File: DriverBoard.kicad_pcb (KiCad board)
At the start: 2 copper layers, 80 x 60 mm, 105 parts, among them J1 Conn_02x07_Odd_Even, J2 Conn_02x07_Odd_Even, Q1 HYG025N06LS1C2, Q2 HYG025N06LS1C2, Q3 HYG025N06LS1C2, Q4 HYG025N06LS1C2, Q5 HYG025N06LS1C2, Q6 HYG025N06LS1C2, U2 SCT2420, U3 SCT2610

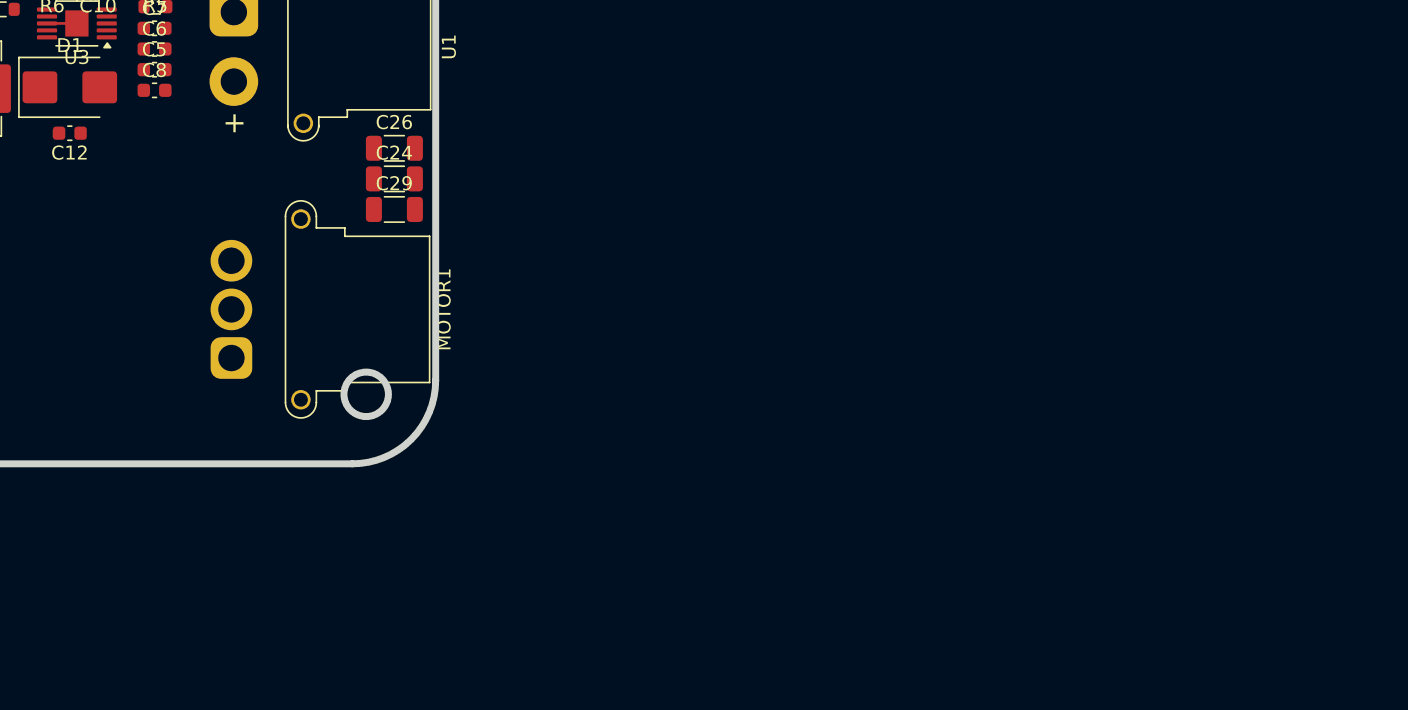
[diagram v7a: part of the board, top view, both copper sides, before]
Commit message: 原理图增加motor2部分
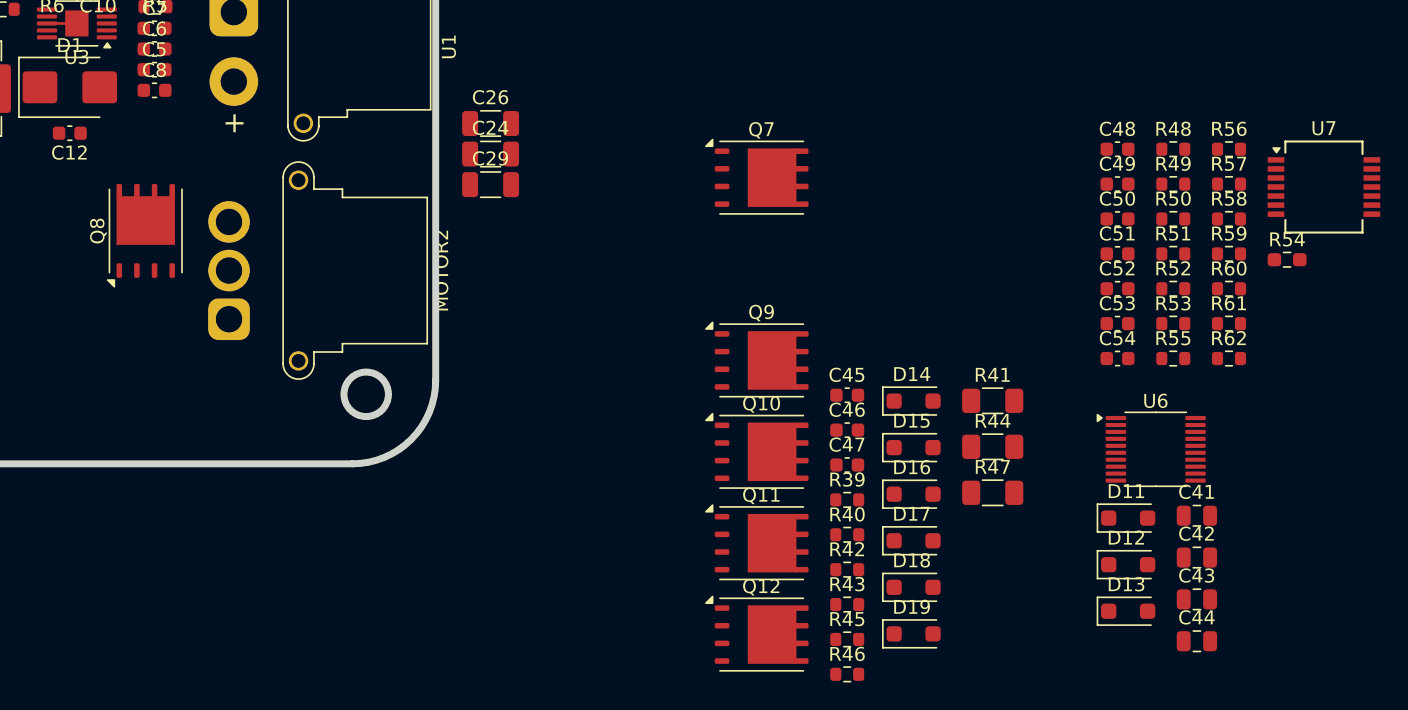
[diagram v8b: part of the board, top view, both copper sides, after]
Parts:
- removed the MOTOR1 at (182.3, 98.6)
- added C41: 0.47uF, Capacitor_SMD:C_0805_2012Metric, F.Cu at (251.7, 109.9)
- added C42: 0.47uF, Capacitor_SMD:C_0805_2012Metric, F.Cu at (251.7, 112.9)
- added C43: 0.47uF, Capacitor_SMD:C_0805_2012Metric, F.Cu at (251.7, 116.0)
- added C44: 0.47uF, Capacitor_SMD:C_0805_2012Metric, F.Cu at (251.7, 119.0)
- added C45: 0.1uF/100V, Capacitor_SMD:C_0603_1608Metric, F.Cu at (226.6, 101.3)
- added C46: 0.1uF/100V, Capacitor_SMD:C_0603_1608Metric, F.Cu at (226.6, 103.8)
- added C47: 0.1uF/100V, Capacitor_SMD:C_0603_1608Metric, F.Cu at (226.6, 106.3)
- added C48: NC, Capacitor_SMD:C_0603_1608Metric, F.Cu at (246.0, 83.6)
- added C49: 1nF, Capacitor_SMD:C_0603_1608Metric, F.Cu at (246.0, 86.1)
- added C50: NC, Capacitor_SMD:C_0603_1608Metric, F.Cu at (246.0, 88.6)
- added C51: NC, Capacitor_SMD:C_0603_1608Metric, F.Cu at (246.0, 91.1)
- added C52: NC, Capacitor_SMD:C_0603_1608Metric, F.Cu at (246.0, 93.6)
- added C53: NC, Capacitor_SMD:C_0603_1608Metric, F.Cu at (246.0, 96.1)
- added C54: NC, Capacitor_SMD:C_0603_1608Metric, F.Cu at (246.0, 98.6)
- added D11: SODF107-SH, Diode_SMD:D_SOD-123F, F.Cu at (246.8, 110.1)
- added D12: SODF107-SH, Diode_SMD:D_SOD-123F, F.Cu at (246.8, 113.5)
- added D13: SODF107-SH, Diode_SMD:D_SOD-123F, F.Cu at (246.8, 116.8)
- added D14: SODF107-SH, Diode_SMD:D_SOD-123F, F.Cu at (231.4, 101.7)
- added D15: SODF107-SH, Diode_SMD:D_SOD-123F, F.Cu at (231.4, 105.0)
- added D16: SODF107-SH, Diode_SMD:D_SOD-123F, F.Cu at (231.4, 108.4)
- added D17: SODF107-SH, Diode_SMD:D_SOD-123F, F.Cu at (231.4, 111.7)
- added D18: SODF107-SH, Diode_SMD:D_SOD-123F, F.Cu at (231.4, 115.1)
- added D19: SODF107-SH, Diode_SMD:D_SOD-123F, F.Cu at (231.4, 118.4)
- added MOTOR2: Conn_01x03, footprints:MR30PW-FB_1x03_P3.50mm_Horizontal, F.Cu at (182.1, 95.8)
- added Q10: HYG025N06LS1C2, footprints:HYG025N06LS1C2-PDFN-8-1EP_6x5mm_P1.27mm_EP3x3mm, F.Cu at (220.4, 105.3)
- added Q11: HYG025N06LS1C2, footprints:HYG025N06LS1C2-PDFN-8-1EP_6x5mm_P1.27mm_EP3x3mm, F.Cu at (220.4, 111.9)
- added Q12: HYG025N06LS1C2, footprints:HYG025N06LS1C2-PDFN-8-1EP_6x5mm_P1.27mm_EP3x3mm, F.Cu at (220.4, 118.5)
- added Q7: HYG025N06LS1C2, footprints:HYG025N06LS1C2-PDFN-8-1EP_6x5mm_P1.27mm_EP3x3mm, F.Cu at (220.4, 85.6)
- added Q8: HYG025N06LS1C2, footprints:HYG025N06LS1C2-PDFN-8-1EP_6x5mm_P1.27mm_EP3x3mm, F.Cu at (176.1, 89.4)
- added Q9: HYG025N06LS1C2, footprints:HYG025N06LS1C2-PDFN-8-1EP_6x5mm_P1.27mm_EP3x3mm, F.Cu at (220.4, 98.8)
- added R39: 100R, Resistor_SMD:R_0603_1608Metric, F.Cu at (226.6, 108.8)
- added R40: 100R, Resistor_SMD:R_0603_1608Metric, F.Cu at (226.6, 111.3)
- added R41: 5mR, Resistor_SMD:R_1206_3216Metric_Pad1.30x1.75mm_HandSolder, F.Cu at (237.0, 101.7)
- added R42: 100R, Resistor_SMD:R_0603_1608Metric, F.Cu at (226.6, 113.8)
- added R43: 100R, Resistor_SMD:R_0603_1608Metric, F.Cu at (226.6, 116.3)
- added R44: 5mR, Resistor_SMD:R_1206_3216Metric_Pad1.30x1.75mm_HandSolder, F.Cu at (237.0, 105.0)
- added R45: 100R, Resistor_SMD:R_0603_1608Metric, F.Cu at (226.6, 118.8)
- added R46: 100R, Resistor_SMD:R_0603_1608Metric, F.Cu at (226.6, 121.3)
- added R47: 5mR, Resistor_SMD:R_1206_3216Metric_Pad1.30x1.75mm_HandSolder, F.Cu at (237.0, 108.3)
- added R48: 4.7K, Resistor_SMD:R_0603_1608Metric, F.Cu at (250.0, 83.6)
- added R49: 4.7K, Resistor_SMD:R_0603_1608Metric, F.Cu at (250.0, 86.1)
- added R50: 6.8K, Resistor_SMD:R_0603_1608Metric, F.Cu at (250.0, 88.6)
- added R51: 1K(1%), Resistor_SMD:R_0603_1608Metric, F.Cu at (250.0, 91.1)
- added R52: 4.7K(1%), Resistor_SMD:R_0603_1608Metric, F.Cu at (250.0, 93.6)
- added R53: 0R, Resistor_SMD:R_0603_1608Metric, F.Cu at (250.0, 96.1)
- added R54: 0.01R, Resistor_SMD:R_0603_1608Metric_Pad0.98x0.95mm_HandSolder, F.Cu at (258.2, 91.5)
- added R55: 6.8K, Resistor_SMD:R_0603_1608Metric, F.Cu at (250.0, 98.6)
- added R56: 1K(1%), Resistor_SMD:R_0603_1608Metric, F.Cu at (254.0, 83.6)
- added R57: 4.7K(1%), Resistor_SMD:R_0603_1608Metric, F.Cu at (254.0, 86.1)
- added R58: 0R, Resistor_SMD:R_0603_1608Metric, F.Cu at (254.0, 88.6)
- added R59: 6.8K, Resistor_SMD:R_0603_1608Metric, F.Cu at (254.0, 91.1)
- added R60: 1K(1%), Resistor_SMD:R_0603_1608Metric, F.Cu at (254.0, 93.6)
- added R61: 4.7K(1%), Resistor_SMD:R_0603_1608Metric, F.Cu at (254.0, 96.1)
- added R62: 0R, Resistor_SMD:R_0603_1608Metric, F.Cu at (254.0, 98.6)
- added U6: FD6288T, Package_SO:TSSOP-20_4.4x5mm_P0.5mm, F.Cu at (248.8, 105.2)
- added U7: ~, Package_SO:SSOP-14_5.3x6.2mm_P0.65mm, F.Cu at (260.9, 86.3)
- U4: value ~ -> FD6288T
- moved C24 7.15 mm to (200.9, 83.9)
- moved C26 7.15 mm to (200.9, 81.7)
- moved C29 7.15 mm to (200.9, 86.1)
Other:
- copper layers 2 -> 4
